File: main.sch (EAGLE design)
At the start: 35 parts, among them IC1 ATTINY13A-SSH, IC2 TP4056-42-ESOP8, IC3 LM27313XMFX_NOPB, T1A 2N4401, T1B NPN, X1 MINI-USB-UX60A-MB-5ST

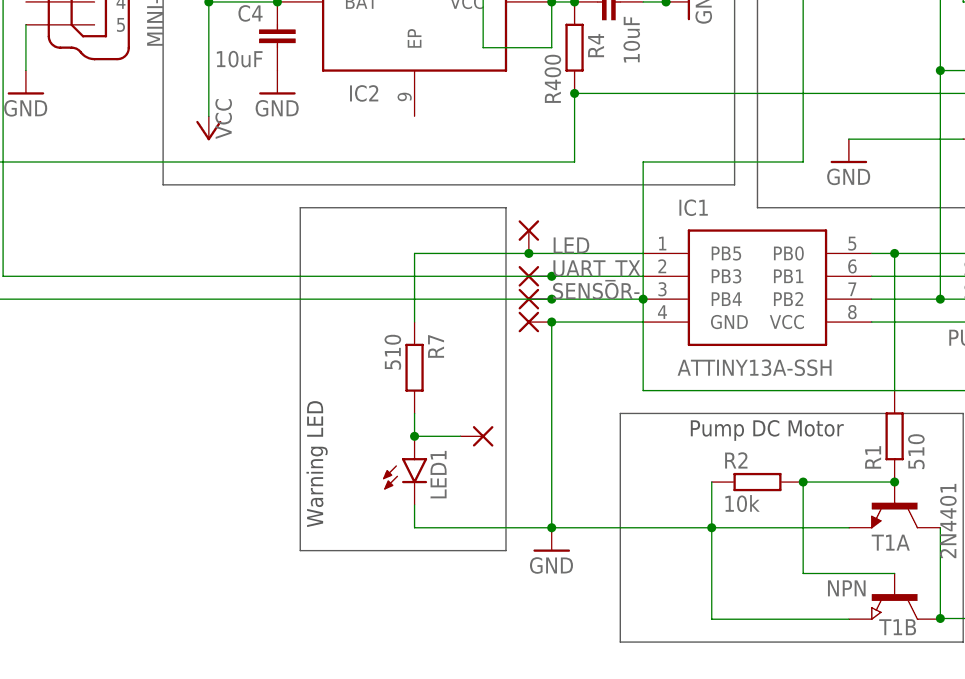
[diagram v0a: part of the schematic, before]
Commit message: solar parameters tuned
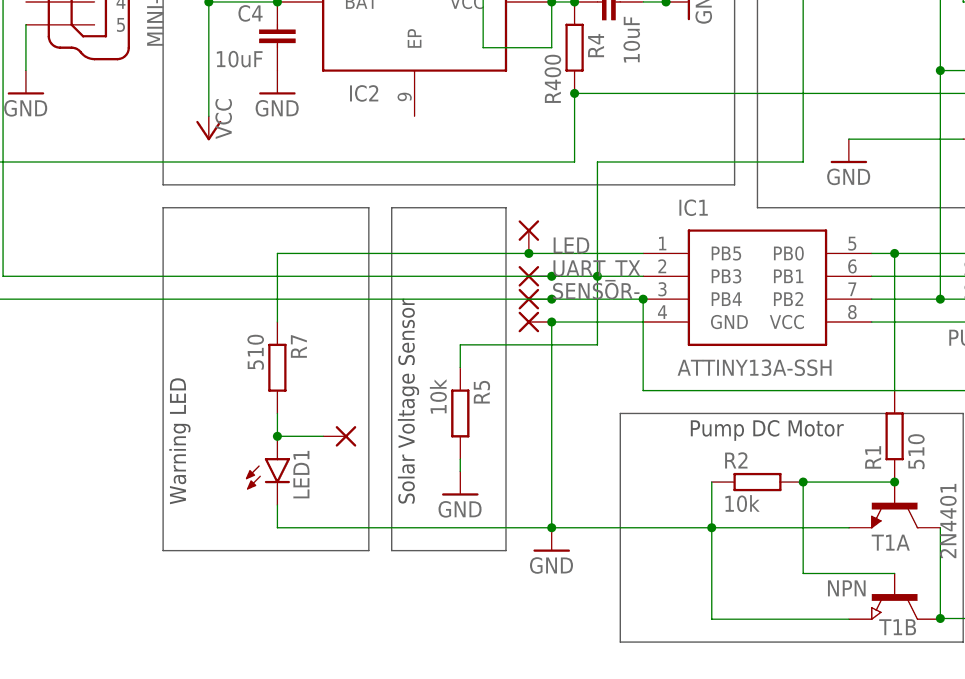
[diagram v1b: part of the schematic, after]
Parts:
- added R5: 10k, resistor:R-EU_M0805
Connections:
- net GND: now also R5.2
- net SENSOR-: no longer R3.1
- net UART_TX: now also R3.1, R5.1
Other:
- note added: "Solar Voltage Sensor"
- moved on the sheet: LED1, R7

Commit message: new graphics
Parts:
- removed BAT+: (no value), wirepad:1,6/0,9
- added X2: 332-02, con-garry:332-02
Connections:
- net VCC: now also X2-1.S; no longer BAT+.P

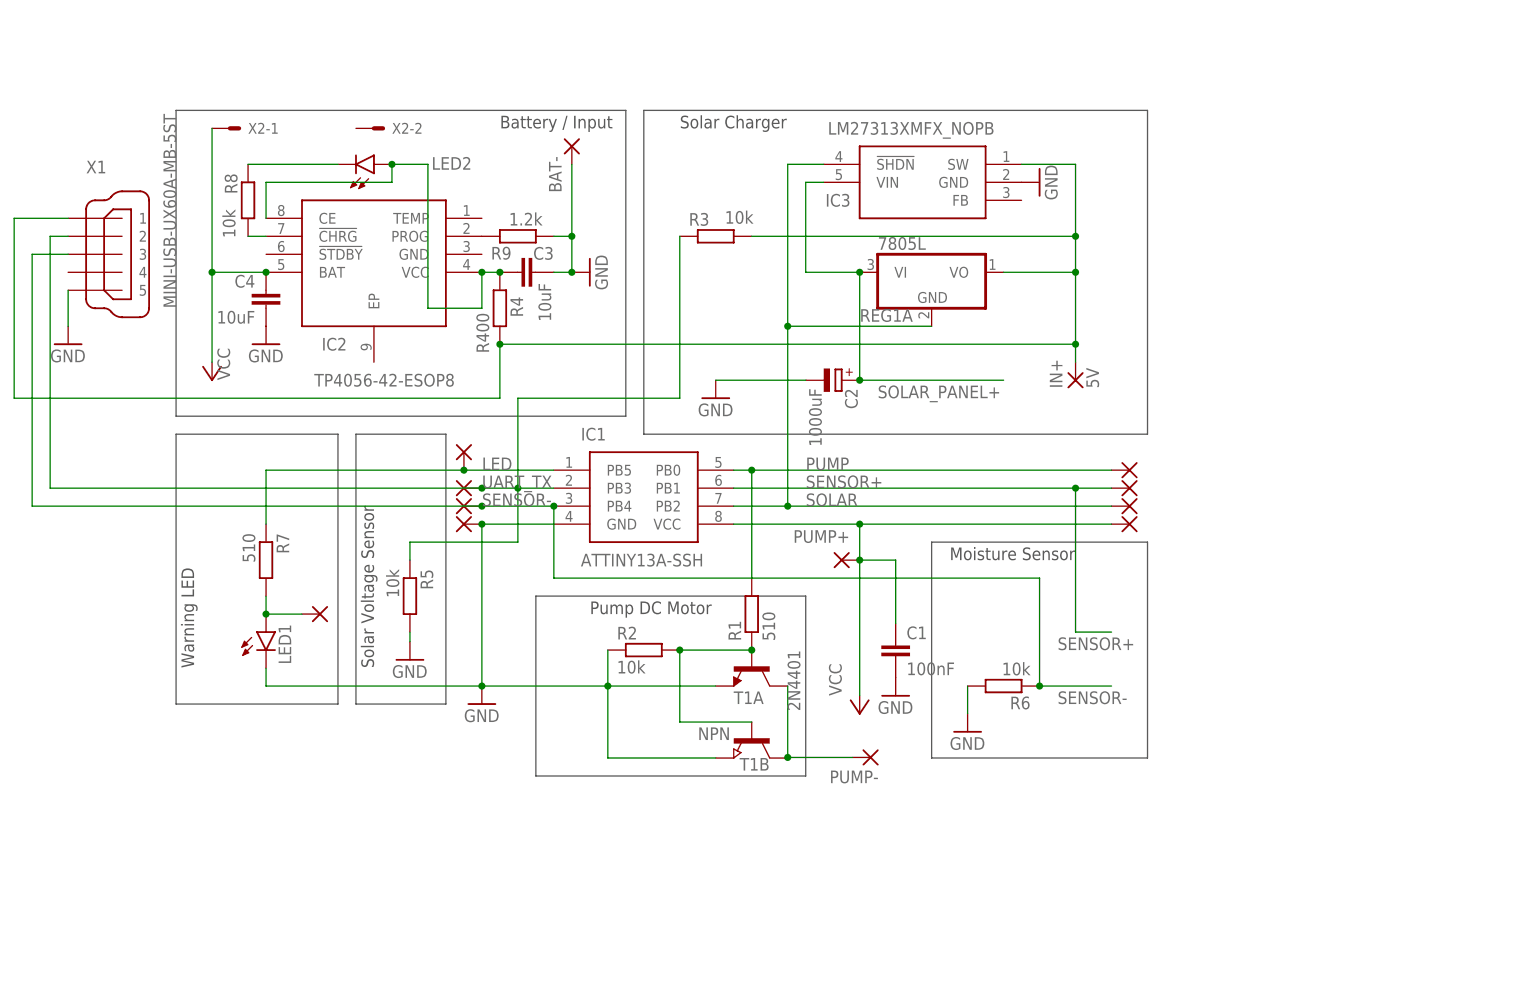
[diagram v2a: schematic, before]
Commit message: removed bootloader added USBasp
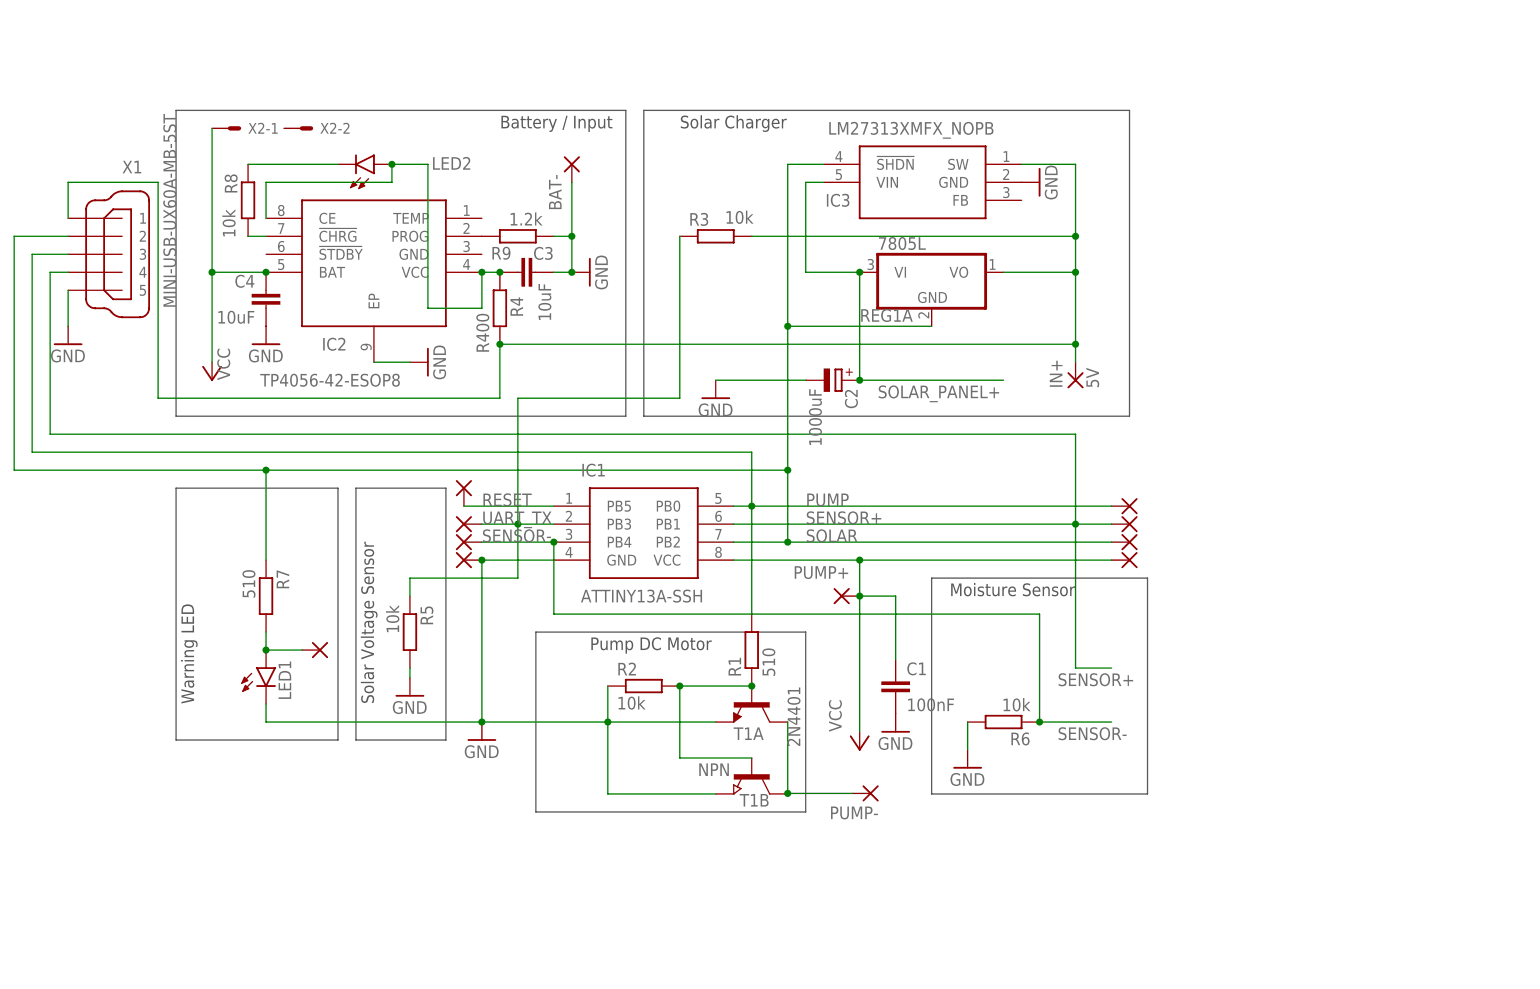
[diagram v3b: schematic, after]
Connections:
- removed net LED: IC1.PB5, PAD10.P, R7.1
- new net RESET: IC1.PB5, PAD10.P
- net GND: now also IC2.EP
- net PUMP: now also X1.3
- net SENSOR+: now also X1.4
- net SENSOR-: no longer X1.3
- net SOLAR: now also R7.1, X1.2
- net UART_TX: no longer X1.2
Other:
- moved on the sheet: BAT-, C1, IC1, LED1, PUMP+, PUMP-, R1, R2, R5, R6, R7, T1A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

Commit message: improved solar
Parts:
- removed BAT-: (no value), wirepad:1,6/0,8
- added B-: (no value), wirepad:1,6/0,8
- added IC4: TPL5110DDCT, SamacSys:TPL5110DDCT
- added R10: 100k, resistor:R-EU_M0805
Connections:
- new net N$3: C1.2, IC1.VCC, IC4.DRV, PAD3.P
- new net N$7: IC4.DELAY/M_DRV, R10.1
- net GND: now also B-.P, C1.1, IC4.GND, R10.2; no longer BAT-.P, C1.2
- net SOLAR: now also IC4.DONE
- net VCC: now also IC4.EN/ONE_SHOT, IC4.VDD; no longer C1.1, IC1.VCC, PAD3.P
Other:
- note added: "Battery / Charger / Input"
- note added: "Low Power Sleep"
- note removed: "Battery / Input"
- moved on the sheet: C1, C2, C3, C4, IC1, IC2, IC3, IN+, LED1, LED2, R1, R2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
